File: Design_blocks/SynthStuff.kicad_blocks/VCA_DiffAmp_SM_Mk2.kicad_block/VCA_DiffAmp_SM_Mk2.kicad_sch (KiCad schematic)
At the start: 20 parts, among them J1 Conn_01x02, J2 Conn_01x04, Q1 BC548, Q2 BC548, U1 TL072

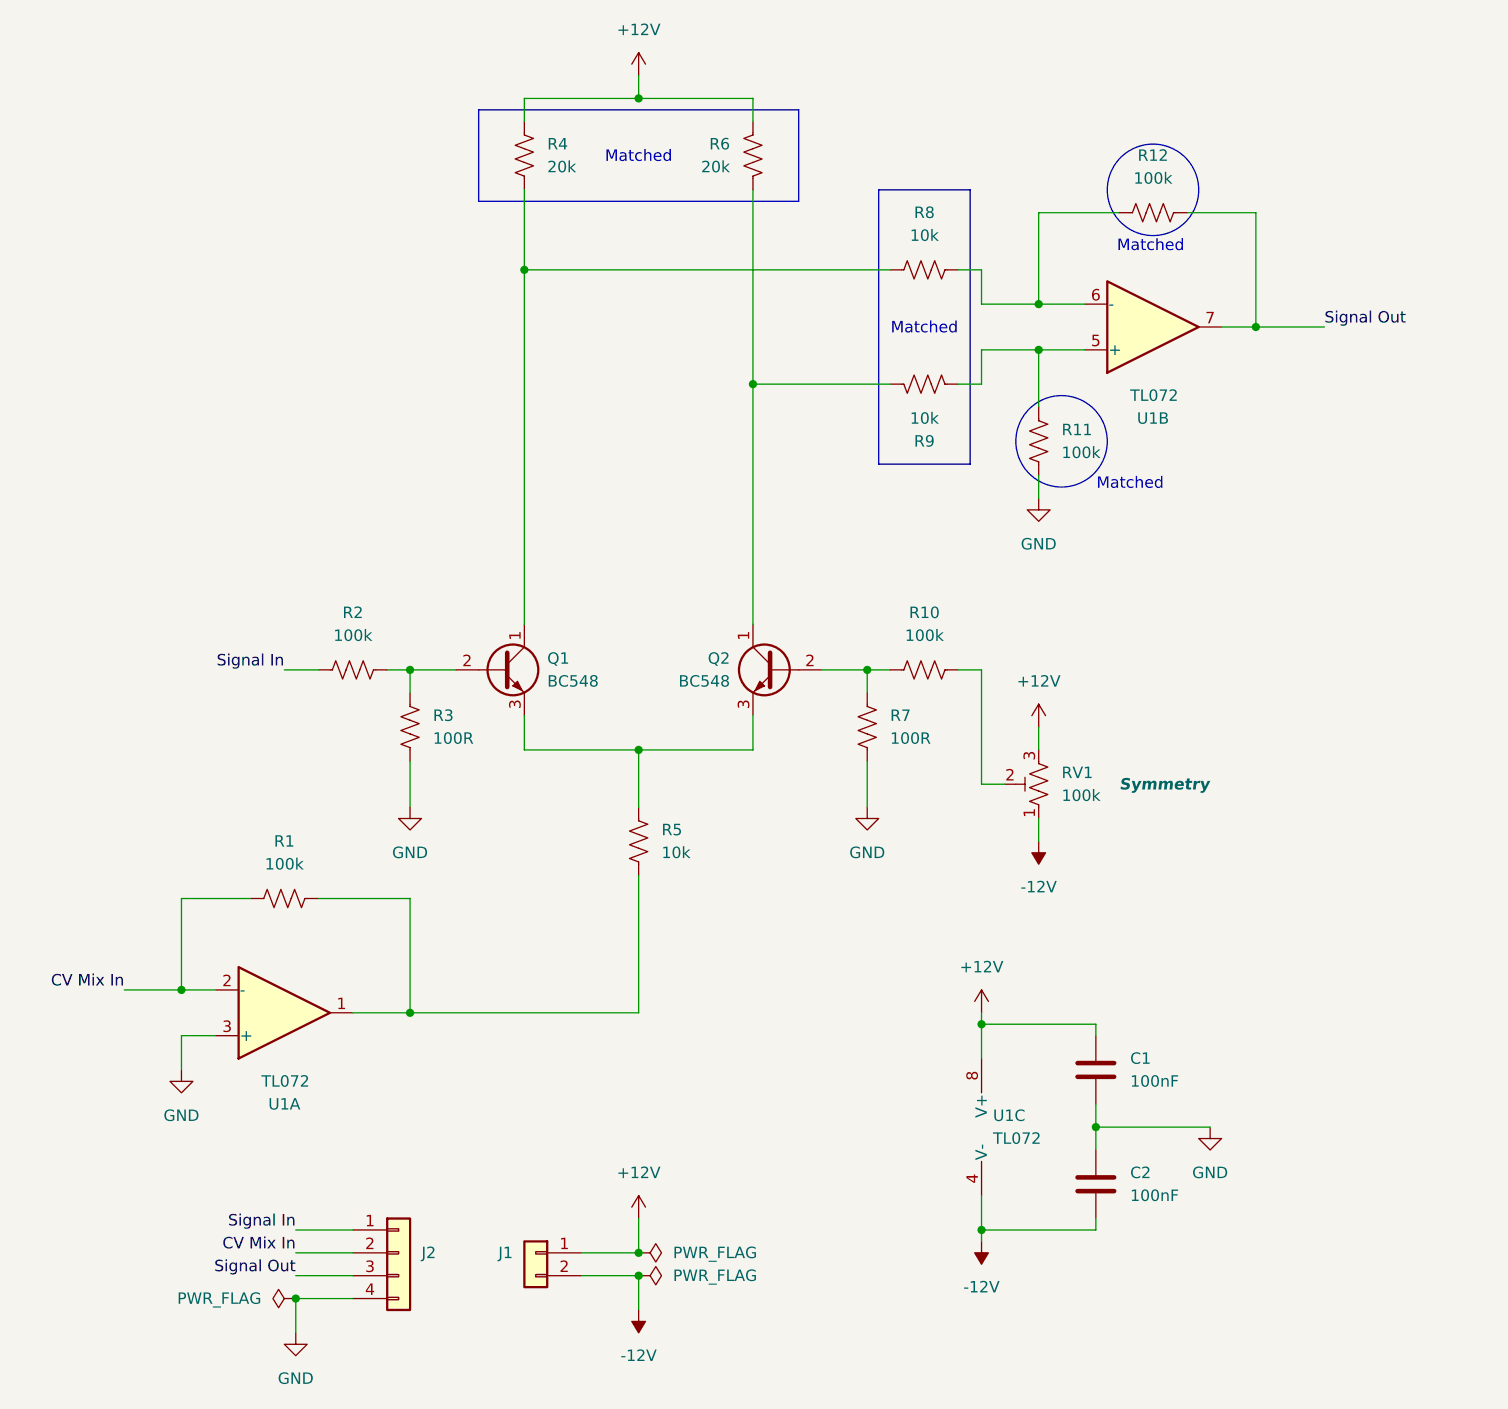
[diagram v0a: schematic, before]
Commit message: VCA minor updates after Mk2 submodule PCB design
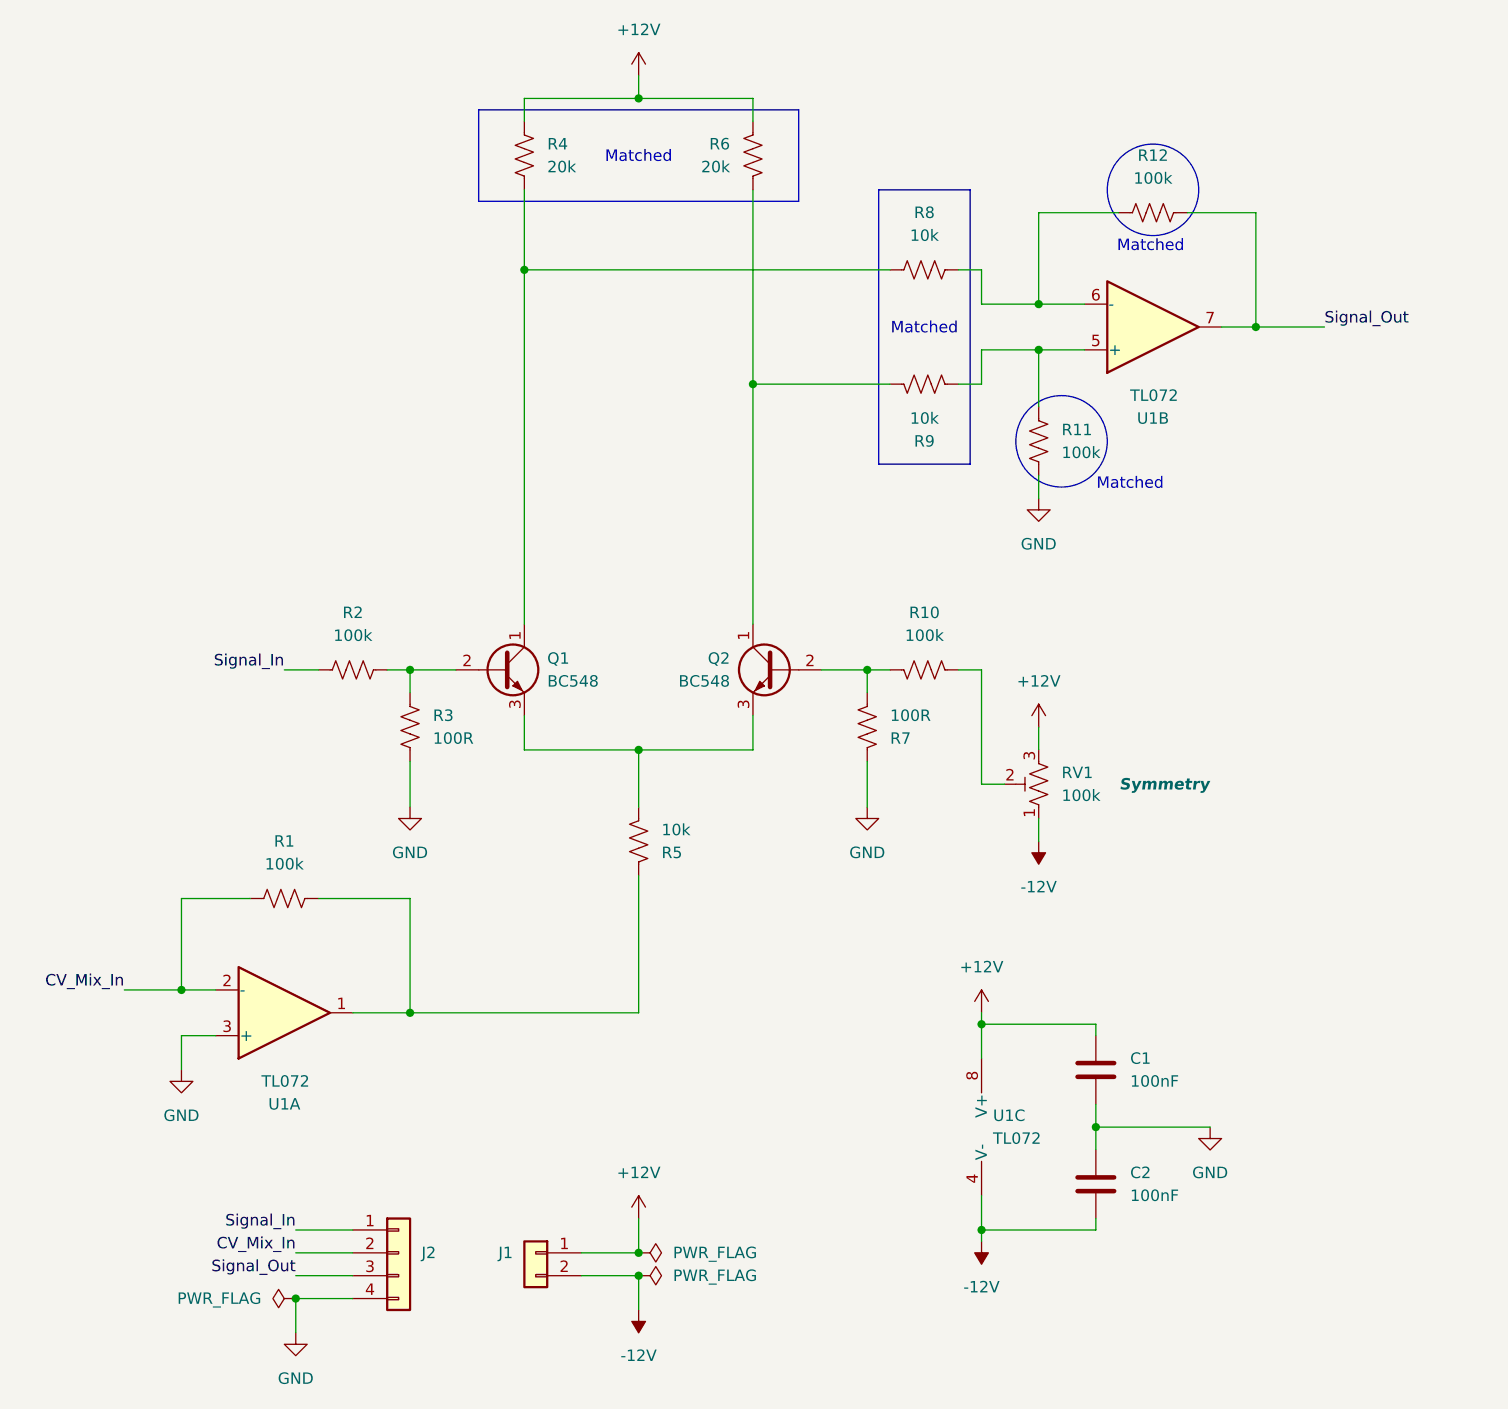
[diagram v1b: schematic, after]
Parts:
- R1, R10, R11, R12, R2, R3, R4, R5, R6, R7, R8, R9: footprint Resistor_THT:R_Axial_DIN0207_L6.3mm_D2.5mm_P7.62mm_Horizontal -> Resistor_THT:R_Axial_DIN0207_L6.3mm_D2.5mm_P2.54mm_Vertical
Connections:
- net GND: now also R7.2; no longer R7.1
- net at R1.2, U1.1: now also R5.2; no longer R5.1
- net at Q1.3 (E), Q2.3 (E): now also R5.1; no longer R5.2
- net at R10.1: now also Q2.2 (B), R7.1; no longer RV1.2
- net CV Mix In renamed CV_Mix_In
- net Signal In renamed Signal_In
- net Signal Out renamed Signal_Out
- new net: R10.2, RV1.2
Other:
- moved on the sheet: R10, R5, R7

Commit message: Updated VCA Mk2 design blocks
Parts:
- added C5: 33pF, Capacitor_THT:C_Disc_D3.4mm_W2.1mm_P2.50mm, symbol Device:C
- added JP1, JP2: SolderJumper_3_Open, Jumper:SolderJumper-3_P1.3mm_Open_RoundedPad1.0x1.5mm_NumberLabels, symbol Jumper:SolderJumper_3_Open
- added TP1: TestPoint_Probe, TestPoint:TestPoint_THTPad_D1.0mm_Drill0.5mm, symbol Connector:TestPoint_Probe
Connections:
- net Signal_Out: now also C5.2, TP1.1
- net at R12.2, R8.1, U1.6 (-): now also C5.1
- net at Q2.1 (C), R6.1: now also JP1.1 (A), JP2.3 (B); no longer R9.2
- net at Q1.1 (C), R4.1: now also JP1.3 (B), JP2.1 (A); no longer R8.2
- new net: JP2.2 (C), R9.2
- new net: JP1.2 (C), R8.2
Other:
- note removed: "Matched"
- moved on the sheet: R8
